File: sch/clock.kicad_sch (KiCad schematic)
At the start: 1 part

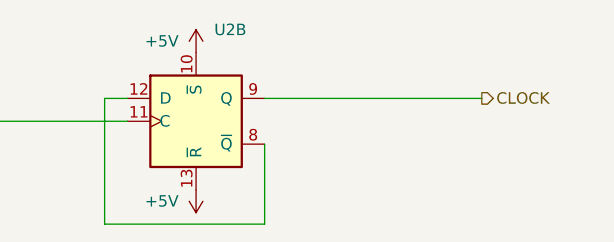
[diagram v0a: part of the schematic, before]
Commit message: Board layout, addr bus
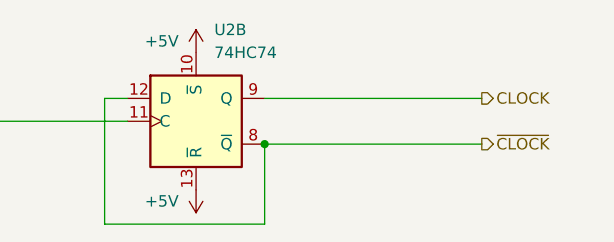
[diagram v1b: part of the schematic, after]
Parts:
- U2: value (none) -> 74HC74; footprint (none) -> Package_SO:SOIC-14_3.9x8.7mm_P1.27mm
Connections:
- net ~{CLOCK}: now reaches U2.12 (D), U2.8 (~{Q})
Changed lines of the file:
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@@
 (kicad_sch (version 20211123) (generator eeschema)
   (paper "A4")
+  (junction (at 128.27 91.44) (diameter 0) (color 0 0 0 0)
+  )
   (wire (pts (xy 88.9 88.9) (xy 113.03 88.9))
     (stroke (width 0) (type default) (color 0 0 0 0))
   )
   (wire (pts (xy 113.03 86.36) (xy 110.49 86.36))
+    (stroke (width 0) (type default) (color 0 0 0 0))
+  )
+  (wire (pts (xy 152.4 91.44) (xy 128.27 91.44))
     (stroke (width 0) (type default) (color 0 0 0 0))
   )
@@
   (hierarchical_label "CRYSTAL" (shape input) (at 88.9 88.9 180)
     (effects (font (size 1.27 1.27)) (justify right))
+  )
+  (hierarchical_label "~{CLOCK}" (shape output) (at 152.4 91.44 0)
+    (effects (font (size 1.27 1.27)) (justify left))
   )
   (hierarchical_label "CLOCK" (shape output) (at 152.4 86.36 0)
@@
       (effects (font (size 1.27 1.27)) (justify left))
     )
-    (property "Value" "" (id 1) (at 122.6694 81.28 0)
+    (property "Value" "74HC74" (id 1) (at 122.6694 81.28 0)
       (effects (font (size 1.27 1.27)) (justify left))
     )
-    (property "Footprint" "" (id 2) (at 120.65 88.9 0)
+    (property "Footprint" "Package_SO:SOIC-14_3.9x8.7mm_P1.27mm" (id 2) (at 120.65 88.9 0)
       (effects (font (size 1.27 1.27)) hide)
     )

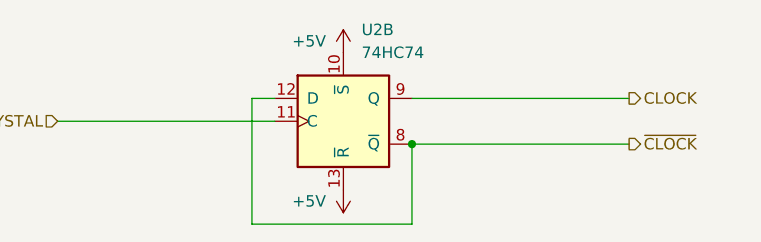
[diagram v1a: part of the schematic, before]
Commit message: More routing, USB iface
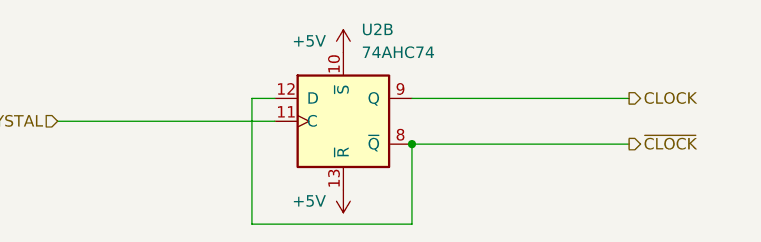
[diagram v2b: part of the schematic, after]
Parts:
- U2: value 74HC74 -> 74AHC74; footprint Package_SO:SOIC-14_3.9x8.7mm_P1.27mm -> Package_SO:TSSOP-14_4.4x5mm_P0.65mm
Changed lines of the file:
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@@
       (effects (font (size 1.27 1.27)) (justify left))
     )
-    (property "Value" "74HC74" (id 1) (at 122.6694 81.28 0)
+    (property "Value" "74AHC74" (id 1) (at 122.6694 81.28 0)
       (effects (font (size 1.27 1.27)) (justify left))
     )
-    (property "Footprint" "Package_SO:SOIC-14_3.9x8.7mm_P1.27mm" (id 2) (at 120.65 88.9 0)
+    (property "Footprint" "Package_SO:TSSOP-14_4.4x5mm_P0.65mm" (id 2) (at 120.65 88.9 0)
       (effects (font (size 1.27 1.27)) hide)
     )
-    (property "Datasheet" "74xx/74hc_hct74.pdf" (id 3) (at 120.65 88.9 0)
+    (property "Datasheet" "https://assets.nexperia.com/documents/data-sheet/74AHC_AHCT74.pdf" (id 3) (at 120.65 88.9 0)
       (effects (font (size 1.27 1.27)) hide)
     )

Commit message: Serial interface
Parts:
- removed U2: 74AHC74, Package_SO:TSSOP-14_4.4x5mm_P0.65mm, symbol 74xx:74LS74
- added C9: (no value), symbol Device:C_Small
- added U2: 74AHC74, Package_SO:TSSOP-14_4.4x5mm_P0.65mm, symbol 74xx:74HC74
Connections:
- net +5V: now also C9.1, U2.1 (~{R}), U2.10 (~{S}), U2.13 (~{R}), U2.14 (VCC), U2.4 (~{S})
- net CLOCK: now also U2.5 (Q)
- net CRYSTAL: now also U2.3 (C)
- net ~{CLOCK}: now also U2.2 (D), U2.6 (~{Q})
- new net GND: C9.2, U2.11 (C), U2.12 (D), U2.7 (GND)
- no-connect marks 0 -> 2
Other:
- company: (none) -> zrthxn
- title: (none) -> 8puter

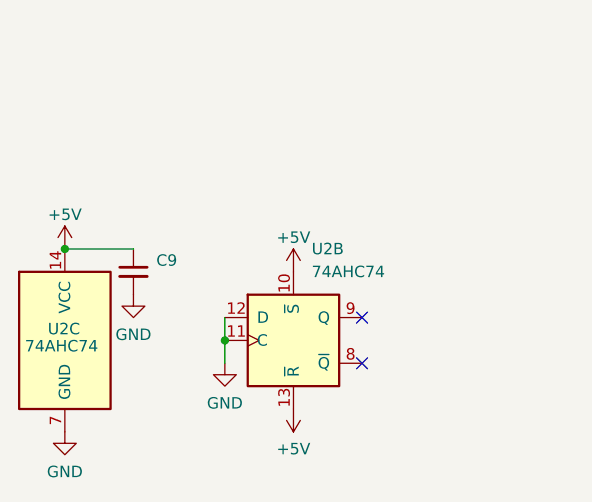
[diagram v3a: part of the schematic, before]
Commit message: Serial, debug and prph headers
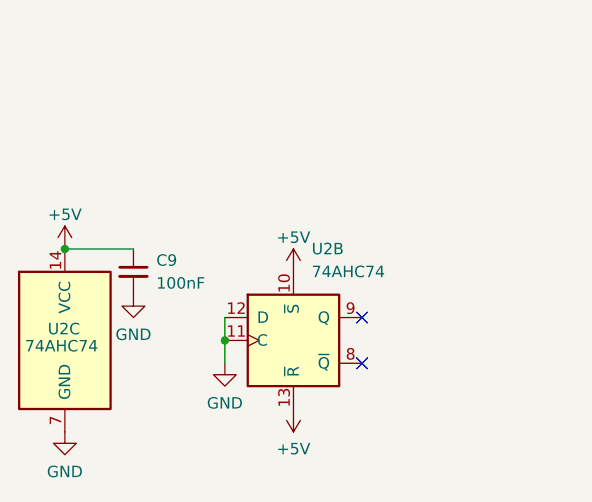
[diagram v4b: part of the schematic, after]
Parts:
- C9: value (none) -> 100nF; footprint (none) -> Capacitor_SMD:C_0805_2012Metric
- U2: footprint (none) -> Package_SO:TSSOP-14_4.4x5mm_P0.65mm
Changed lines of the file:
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@@
       (effects (font (size 1.27 1.27)) (justify left))
     )
-    (property "Footprint" "" (id 2) (at 58.42 173.355 0)
+    (property "Footprint" "Package_SO:TSSOP-14_4.4x5mm_P0.65mm" (id 2) (at 58.42 173.355 0)
       (effects (font (size 1.27 1.27)) hide)
     )
@@
       (effects (font (size 1.27 1.27)) (justify left))
     )
-    (property "Value" "" (id 1) (at 43.18 167.0112 0)
+    (property "Value" "100nF" (id 1) (at 43.18 167.0112 0)
       (effects (font (size 1.27 1.27)) (justify left))
     )
-    (property "Footprint" "" (id 2) (at 40.64 165.735 0)
+    (property "Footprint" "Capacitor_SMD:C_0805_2012Metric" (id 2) (at 40.64 165.735 0)
       (effects (font (size 1.27 1.27)) hide)
     )
@@
       (effects (font (size 1.27 1.27)) (justify left))
     )
-    (property "Footprint" "" (id 2) (at 33.02 173.355 0)
+    (property "Footprint" "Package_SO:TSSOP-14_4.4x5mm_P0.65mm" (id 2) (at 33.02 173.355 0)
       (effects (font (size 1.27 1.27)) hide)
     )

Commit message: First completed routing
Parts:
- added C18: (no value), symbol Device:C_Small
- added CS_SEL1: (no value), symbol Connector_Generic:Conn_02x03_Odd_Even
- added R30, R31: (no value), symbol Device:R
- added STEP_SW1: PUSHBTN, Button_Switch_THT:SW_PUSH_6mm_H13mm, symbol Switch:SW_Push
- added U3: (no value), symbol 74xGxx:SN74LVC1G14DBV
- U2: value 74AHC74 -> (none); footprint Package_SO:TSSOP-14_4.4x5mm_P0.65mm -> (none)
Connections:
- net +5V: now also STEP_SW1.2, U3.5 (VCC)
- net CLOCK: now also CS_SEL1.2 (Pin_2), CS_SEL1.4 (Pin_4), CS_SEL1.6 (Pin_6); no longer U2.5 (Q)
- net GND: now also C18.2, CS_SEL1.5 (Pin_5), R30.1, U3.3 (GND); no longer U2.11 (C), U2.12 (D)
- net at U2.8 (~{Q}): now also U2.12 (D)
- net STEP: now reaches U2.9 (Q)
- net STEP: now also CS_SEL1.3 (Pin_3)
- net ~{CLOCK}: no longer names the net of U2.2 (D), U2.6 (~{Q})
- new net: U2.11 (C), U3.4
- new net: C18.1, R31.2, U3.2
- new net: R30.2, R31.1, STEP_SW1.1
- new net OSCC: CS_SEL1.1 (Pin_1), U2.5 (Q)
- no-connect marks 2 -> 0
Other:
- moved on the sheet: C9, U2A, U2B, U2C

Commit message: Gerber Plots
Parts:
- C18: value (none) -> 1uF; footprint (none) -> Capacitor_SMD:C_0805_2012Metric
- CS_SEL1: value (none) -> Conn_02x03_Odd_Even; footprint (none) -> Connector_PinHeader_2.00mm:PinHeader_2x03_P2.00mm_Vertical
- R30: value (none) -> 10K; footprint (none) -> Resistor_SMD:R_0805_2012Metric
- R31: value (none) -> 47K; footprint (none) -> Resistor_SMD:R_0805_2012Metric
- U2: value (none) -> 74AHC74; footprint (none) -> Package_SO:TSSOP-14_4.4x5mm_P0.65mm
- U3: value (none) -> SN74LVC1G14DBV; footprint (none) -> Package_TO_SOT_SMD:SOT-23-5
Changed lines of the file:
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@@
     (in_bom yes) (on_board yes) (fields_autoplaced)
     (property "Reference" "CS_SEL1" (id 0) (at 144.78 43.18 0))
-    (property "Value" "" (id 1) (at 144.78 45.72 0))
-    (property "Footprint" "" (id 2) (at 143.51 52.07 0)
+    (property "Value" "Conn_02x03_Odd_Even" (id 1) (at 144.78 45.72 0))
+    (property "Footprint" "Connector_PinHeader_2.00mm:PinHeader_2x03_P2.00mm_Vertical" (id 2) (at 143.51 52.07 0)
       (effects (font (size 1.27 1.27)) hide)
     )
@@
       (effects (font (size 1.27 1.27)) (justify left))
     )
-    (property "Value" "" (id 1) (at 76.3144 40.64 0)
-      (effects (font (size 1.27 1.27)) (justify left))
-    )
-    (property "Footprint" "" (id 2) (at 74.295 48.26 0)
+    (property "Value" "74AHC74" (id 1) (at 76.3144 40.64 0)
+      (effects (font (size 1.27 1.27)) (justify left))
+    )
+    (property "Footprint" "Package_SO:TSSOP-14_4.4x5mm_P0.65mm" (id 2) (at 74.295 48.26 0)
       (effects (font (size 1.27 1.27)) hide)
     )
@@
       (effects (font (size 1.27 1.27)) hide)
     )
-    (property "Value" "" (id 1) (at 92.075 82.55 0))
+    (property "Value" "+5V" (id 1) (at 92.075 82.55 0))
     (property "Footprint" "" (id 2) (at 92.075 86.36 0)
       (effects (font (size 1.27 1.27)) hide)
@@
       (effects (font (size 1.27 1.27)) hide)
     )
-    (property "Value" "" (id 1) (at 92.075 101.6 0))
+    (property "Value" "GND" (id 1) (at 92.075 101.6 0))
     (property "Footprint" "" (id 2) (at 92.075 96.52 0)
       (effects (font (size 1.27 1.27)) hide)
@@
       (effects (font (size 1.27 1.27)) (justify left))
     )
-    (property "Value" "" (id 1) (at 115.0494 83.82 0)
-      (effects (font (size 1.27 1.27)) (justify left))
-    )
-    (property "Footprint" "" (id 2) (at 113.03 91.44 0)
+    (property "Value" "74AHC74" (id 1) (at 115.0494 83.82 0)
+      (effects (font (size 1.27 1.27)) (justify left))
+    )
+    (property "Footprint" "Package_SO:TSSOP-14_4.4x5mm_P0.65mm" (id 2) (at 113.03 91.44 0)
       (effects (font (size 1.27 1.27)) hide)
     )
@@
     (in_bom yes) (on_board yes)
     (property "Reference" "U3" (id 0) (at 92.075 76.2 0))
-    (property "Value" "" (id 1) (at 92.075 78.74 0))
-    (property "Footprint" "" (id 2) (at 92.075 97.79 0)
+    (property "Value" "SN74LVC1G14DBV" (id 1) (at 92.075 78.74 0))
+    (property "Footprint" "Package_TO_SOT_SMD:SOT-23-5" (id 2) (at 92.075 97.79 0)
       (effects (font (size 1.27 1.27)) hide)
     )
@@
       (effects (font (size 1.27 1.27)) hide)
     )
-    (property "Value" "" (id 1) (at 132.715 59.055 0))
+    (property "Value" "GND" (id 1) (at 132.715 59.055 0))
     (property "Footprint" "" (id 2) (at 132.715 54.61 0)
       (effects (font (size 1.27 1.27)) hide)
@@
     (in_bom yes) (on_board yes)
     (property "Reference" "R31" (id 0) (at 74.295 86.995 90))
-    (property "Value" "" (id 1) (at 74.295 88.9 90))
-    (property "Footprint" "" (id 2) (at 74.295 93.218 90)
+    (property "Value" "47K" (id 1) (at 74.295 88.9 90))
+    (property "Footprint" "Resistor_SMD:R_0805_2012Metric" (id 2) (at 74.295 93.218 90)
       (effects (font (size 1.27 1.27)) hide)
     )
@@
       (effects (font (size 1.27 1.27)) hide)
     )
-    (property "Value" "" (id 1) (at 63.5 77.47 0))
+    (property "Value" "+5V" (id 1) (at 63.5 77.47 0))
     (property "Footprint" "" (id 2) (at 63.5 81.28 0)
       (effects (font (size 1.27 1.27)) hide)
@@
       (effects (font (size 1.27 1.27)) (justify left))
     )
-    (property "Value" "" (id 1) (at 76.2 97.79 0)
-      (effects (font (size 1.27 1.27)) (justify left))
-    )
-    (property "Footprint" "" (id 2) (at 82.55 96.52 0)
+    (property "Value" "1uF" (id 1) (at 76.2 97.79 0)
+      (effects (font (size 1.27 1.27)) (justify left))
+    )
+    (property "Footprint" "Capacitor_SMD:C_0805_2012Metric" (id 2) (at 82.55 96.52 0)
       (effects (font (size 1.27 1.27)) hide)
     )
@@
       (effects (font (size 1.27 1.27)) (justify right))
     )
-    (property "Value" "" (id 1) (at 57.785 96.52 0)
+    (property "Value" "10K" (id 1) (at 57.785 96.52 0)
       (effects (font (size 1.27 1.27)) (justify right))
     )
-    (property "Footprint" "" (id 2) (at 65.278 95.25 90)
+    (property "Footprint" "Resistor_SMD:R_0805_2012Metric" (id 2) (at 65.278 95.25 90)
       (effects (font (size 1.27 1.27)) hide)
     )
@@
       (effects (font (size 1.27 1.27)) (justify left))
     )
-    (property "Value" "" (id 1) (at 59.055 165.735 0)
-      (effects (font (size 1.27 1.27)) (justify left))
-    )
-    (property "Footprint" "" (id 2) (at 63.5 165.1 0)
-      (effects (font (size 1.27 1.27)) hide)
-    )
+    (property "Value" "74AHC74" (id 1) (at 59.055 165.735 0)
+      (effects (font (size 1.27 1.27)) (justify left))
+    )
+    (property "Footprint" "Package_SO:TSSOP-14_4.4x5mm_P0.65mm" (id 2) (at 63.5 165.1 0)
+      (effects (font (size 1.27 1.27)) hide)
+    )

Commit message: board improvements
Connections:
- net GND: no longer CS_SEL1.5 (Pin_5)
- no-connect marks 0 -> 1
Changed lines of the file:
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@@
   (junction (at 63.5 154.94) (diameter 0) (color 0 0 0 0)
   )
+  (no_connect (at 138.43 54.61))
   (wire (pts (xy 102.87 102.87) (xy 120.65 102.87))
     (stroke (width 0) (type default) (color 0 0 0 0))
@@
   )
   (wire (pts (xy 132.715 49.53) (xy 138.43 49.53))
-    (stroke (width 0) (type default) (color 0 0 0 0))
-  )
-  (wire (pts (xy 132.715 54.61) (xy 138.43 54.61))
     (stroke (width 0) (type default) (color 0 0 0 0))
   )
@@
       (effects (font (size 1.27 1.27)) hide)
     )
-    (pin "1")
-  )
-  (symbol (lib_id "power:GND") (at 132.715 54.61 0) (unit 1)
-    (in_bom yes) (on_board yes) (fields_autoplaced)
-    (property "Reference" "#PWR021" (id 0) (at 132.715 60.96 0)
-      (effects (font (size 1.27 1.27)) hide)
-    )
-    (property "Value" "GND" (id 1) (at 132.715 59.055 0))
-    (property "Footprint" "" (id 2) (at 132.715 54.61 0)
-      (effects (font (size 1.27 1.27)) hide)
-    )
-    (property "Datasheet" "" (id 3) (at 132.715 54.61 0)
-      (effects (font (size 1.27 1.27)) hide)
-    )

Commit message: some docs
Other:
- note added: "Clicking the button will take us to the next HALF clock cycle."
- note added: "Clock Source Select"
- moved on the sheet: C18, C9, CS_SEL1, R30, R31, STEP_SW1, U2B, U2C, U3
